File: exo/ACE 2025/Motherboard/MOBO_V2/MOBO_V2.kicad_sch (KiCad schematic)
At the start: 0 parts

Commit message: push schema électrique
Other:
- sheet ESP32_SD renamed ESP32_SD_EXTRA
- added sheet Connecteurs (Connecteurs.kicad_sch)
- sheet CAN ports: added CAN_N, CAN_P, RS232_RX, RS232_TX; removed none
- sheet ESP32_SD_EXTRA: file ESP32_SD.kicad_sch -> ESP32_SD_EXTRA.kicad_sch
- sheet I2C_w_Protection ports: added DOS{SDA[1..2] SCL[1..2]}, D{SDA[1..2] SCL[1..2]}, G{SDA[1..2] SCL[1..2]}; removed none
- note added: "BMS"
- note added: "BNO085 cuisse"
- note added: "BNO085 dos"
- note added: "BNO085 tibia"
- note added: "Batterie 48V"
- note added: "Batterie pack 5V"
- note added: "CAN/UART"
- note added: "CAN/UART ou Diff I2C?"
- note added: "Diff I2C"
- note added: "ETH"
- note added: "MOBO"
- note added: "Montre intelligente"
- note added: "Moteur Genou"
- note added: "Moteur Hanche"
- note added: "Moustcahe jambe droite"
- note added: "Moustcahe jambe gauche"
- note added: "Sans fil"
- note added: "SoM ESP32-S3"
- note added: "USB-C"

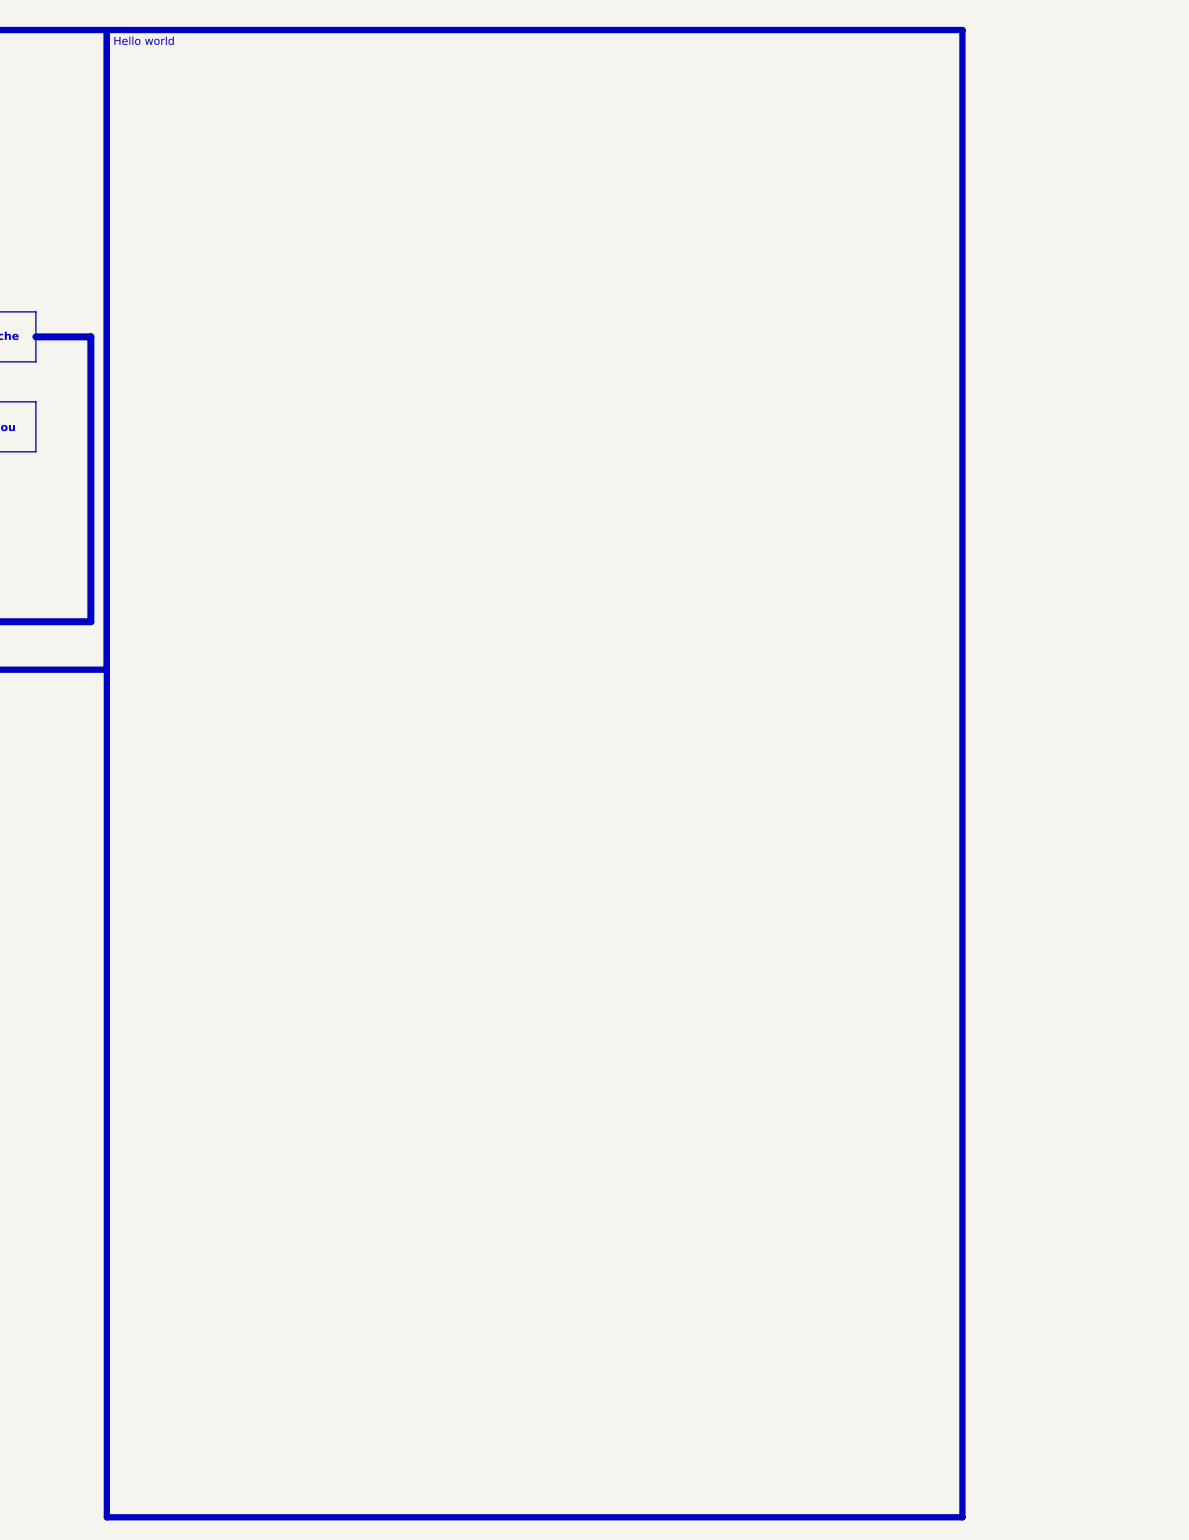
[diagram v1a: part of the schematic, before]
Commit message: ajout infromation et d'épaisseur des traces selon le netclass et de joli couleur hehe
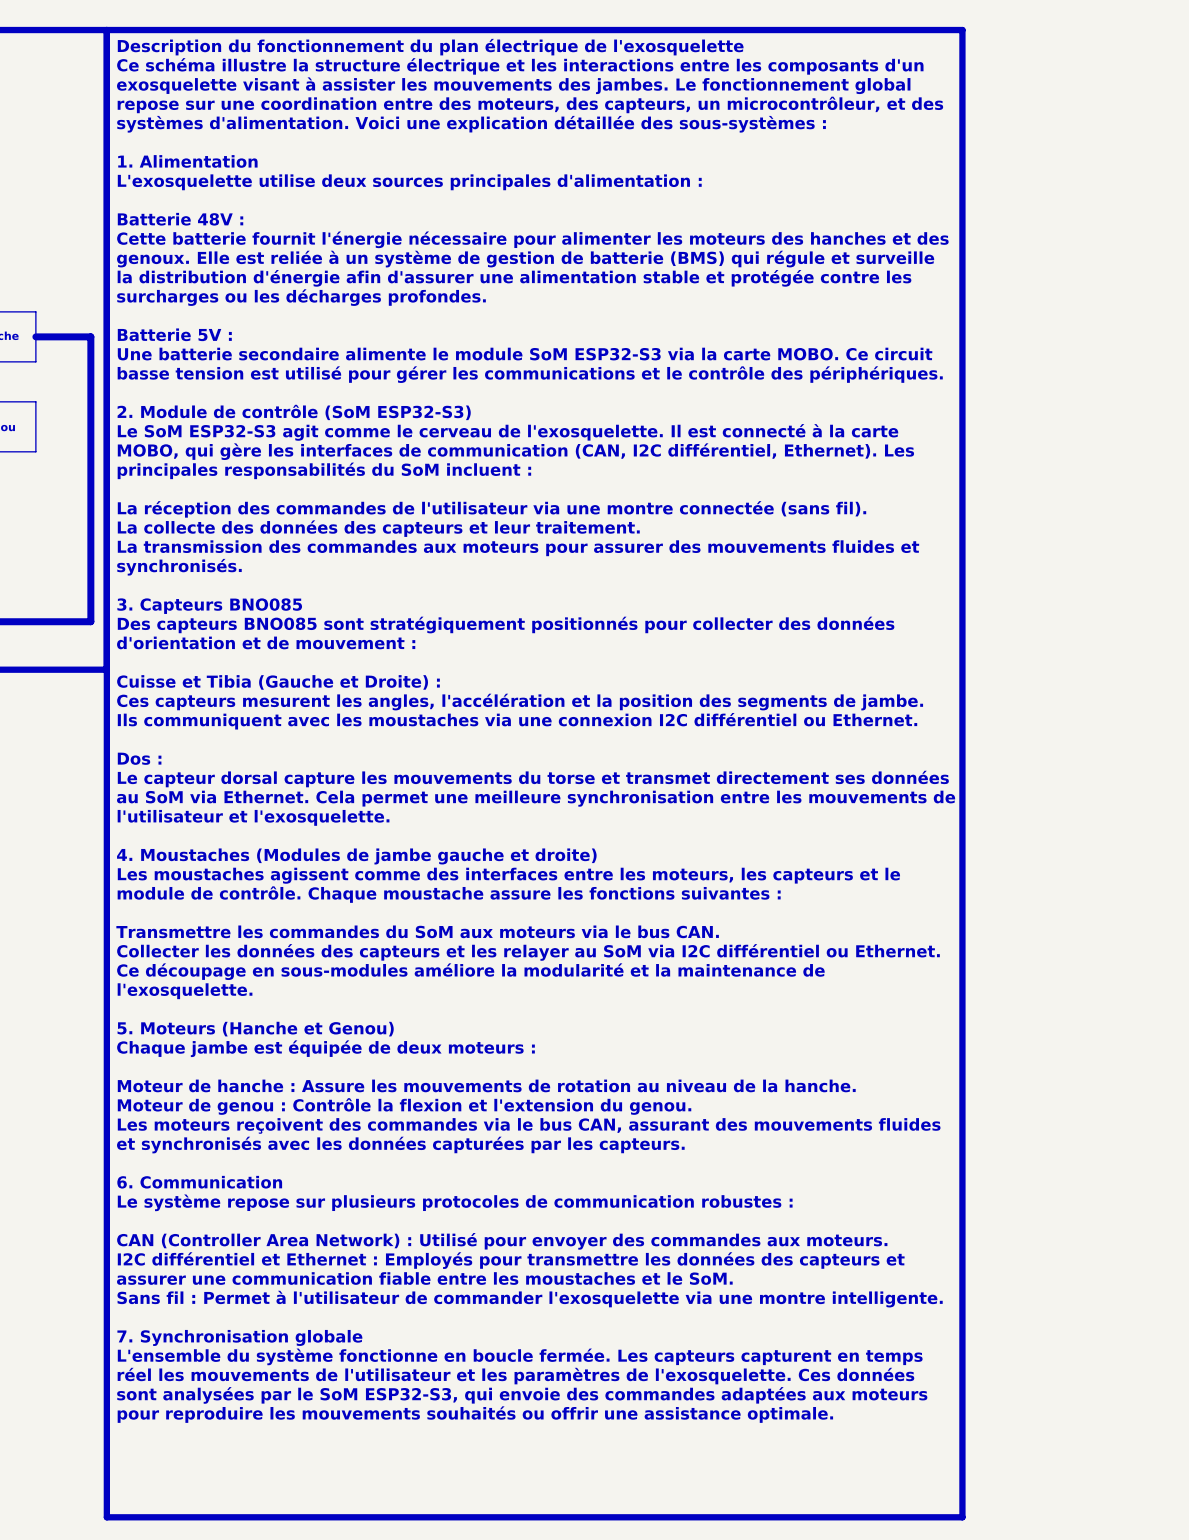
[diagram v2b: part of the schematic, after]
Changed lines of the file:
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@@
 		)
 	)
-	(text_box "Hello world"
+	(text_box "Description du fonctionnement du plan électrique de l'exosquelette\nCe schéma illustre la structure électrique et les interactions entre les composants d'un exosquelette visant à assister les mouvements des jambes. Le fonctionnement global repose sur une coordination entre des moteurs, des capteurs, un microcontrôleur, et des systèmes d'alimentation. Voici une explication détaillée des sous-systèmes :\n\n1. Alimentation\nL'exosquelette utilise deux sources principales d'alimentation :\n\nBatterie 48V :\nCette batterie fournit l'énergie nécessaire pour alimenter les moteurs des hanches et des genoux. Elle est reliée à un système de gestion de batterie (BMS) qui régule et surveille la distribution d'énergie afin d'assurer une alimentation stable et protégée contre les surcharges ou les décharges profondes.\n\nBatterie 5V :\nUne batterie secondaire alimente le module SoM ESP32-S3 via la carte MOBO. Ce circuit basse tension est utilisé pour gérer les communications et le contrôle des périphériques.\n\n2. Module de contrôle (SoM ESP32-S3)\nLe SoM ESP32-S3 agit comme le cerveau de l'exosquelette. Il est connecté à la carte MOBO, qui gère les interfaces de communication (CAN, I2C différentiel, Ethernet). Les principales responsabilités du SoM incluent :\n\nLa réception des commandes de l'utilisateur via une montre connectée (sans fil).\nLa collecte des données des capteurs et leur traitement.\nLa transmission des commandes aux moteurs pour assurer des mouvements fluides et synchronisés.\n\n3. Capteurs BNO085\nDes capteurs BNO085 sont stratégiquement positionnés pour collecter des données d'orientation et de mouvement :\n\nCuisse et Tibia (Gauche et Droite) :\nCes capteurs mesurent les angles, l'accélération et la position des segments de jambe. Ils communiquent avec les moustaches via une connexion I2C différentiel ou Ethernet.\n\nDos :\nLe capteur dorsal capture les mouvements du torse et transmet directement ses données au SoM via Ethernet. Cela permet une meilleure synchronisation entre les mouvements de l'utilisateur et l'exosquelette.\n\n4. Moustaches (Modules de jambe gauche et droite)\nLes moustaches agissent comme des interfaces entre les moteurs, les capteurs et le module de contrôle. Chaque moustache assure les fonctions suivantes :\n\nTransmettre les commandes du SoM aux moteurs via le bus CAN.\nCollecter les données des capteurs et les relayer au SoM via I2C différentiel ou Ethernet.\nCe découpage en sous-modules améliore la modularité et la maintenance de l'exosquelette.\n\n5. Moteurs (Hanche et Genou)\nChaque jambe est équipée de deux moteurs :\n\nMoteur de hanche : Assure les mouvements de rotation au niveau de la hanche.\nMoteur de genou : Contrôle la flexion et l'extension du genou.\nLes moteurs reçoivent des commandes via le bus CAN, assurant des mouvements fluides et synchronisés avec les données capturées par les capteurs.\n\n6. Communication\nLe système repose sur plusieurs protocoles de communication robustes :\n\nCAN (Controller Area Network) : Utilisé pour envoyer des commandes aux moteurs.\nI2C différentiel et Ethernet : Employés pour transmettre les données des capteurs et assurer une communication fiable entre les moustaches et le SoM.\nSans fil : Permet à l'utilisateur de commander l'exosquelette via une montre intelligente.\n\n7. Synchronisation globale\nL'ensemble du système fonctionne en boucle fermée. Les capteurs capturent en temps réel les mouvements de l'utilisateur et les paramètres de l'exosquelette. Ces données sont analysées par le SoM ESP32-S3, qui envoie des commandes adaptées aux moteurs pour reproduire les mouvements souhaités ou offrir une assistance optimale."
 		(exclude_from_sim no)
 		(at 270.51 15.24 0)
@@
 		(effects
 			(font
-				(size 1.27 1.27)
-				(color 61 112 78 1)
+				(size 1.9 1.9)
+				(thickness 0.3)
+				(bold yes)
+				(color 41 75 52 1)
 			)
 			(justify left top)
